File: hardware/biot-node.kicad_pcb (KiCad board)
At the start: 2 copper layers, 36.8 x 29 mm, 11 parts, among them J1 MPU9250 connection, J2 3.3V DC, P1 ATSAMR21B, P2 ATSAMR21B-TEST-POINTs, P3 ATMEL-CORTEX, P4 FTDI/Serial, SW1 Reset

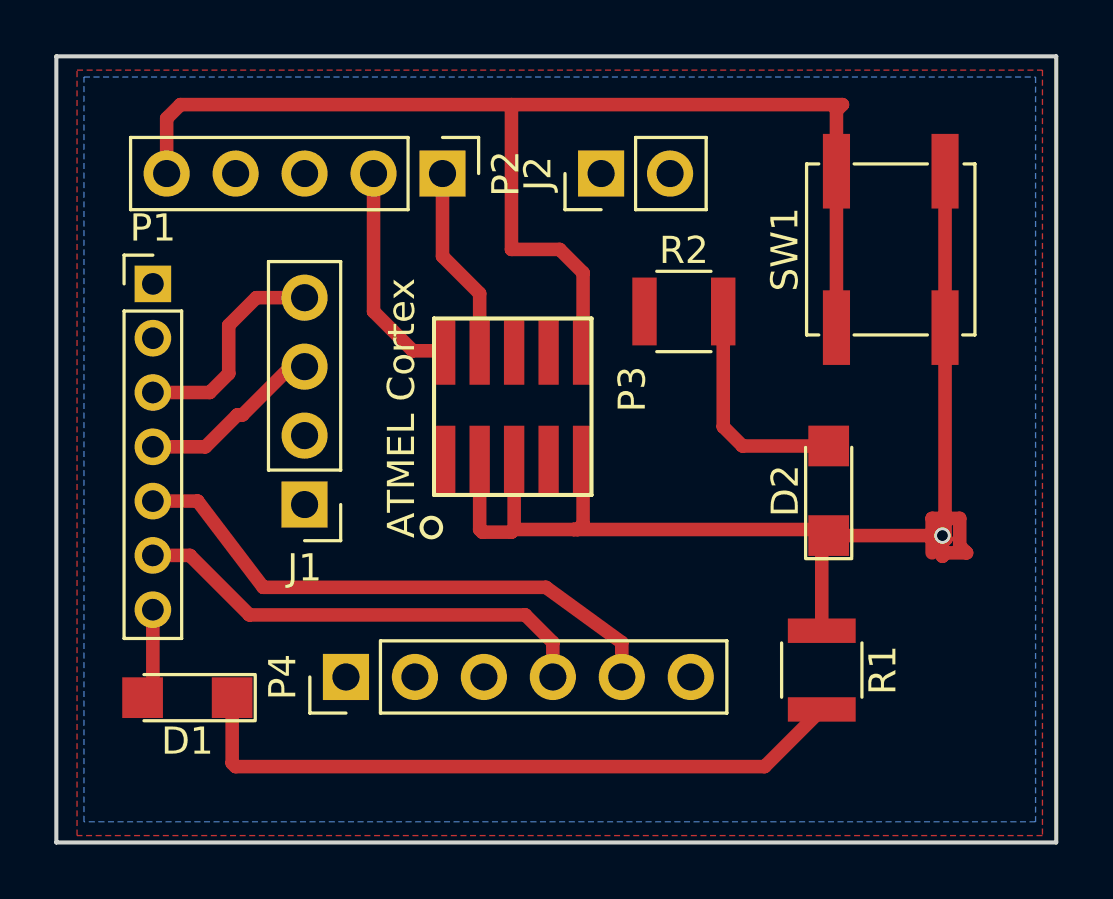
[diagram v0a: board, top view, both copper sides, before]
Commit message: Modifying PCB to suit my fabrication tools.
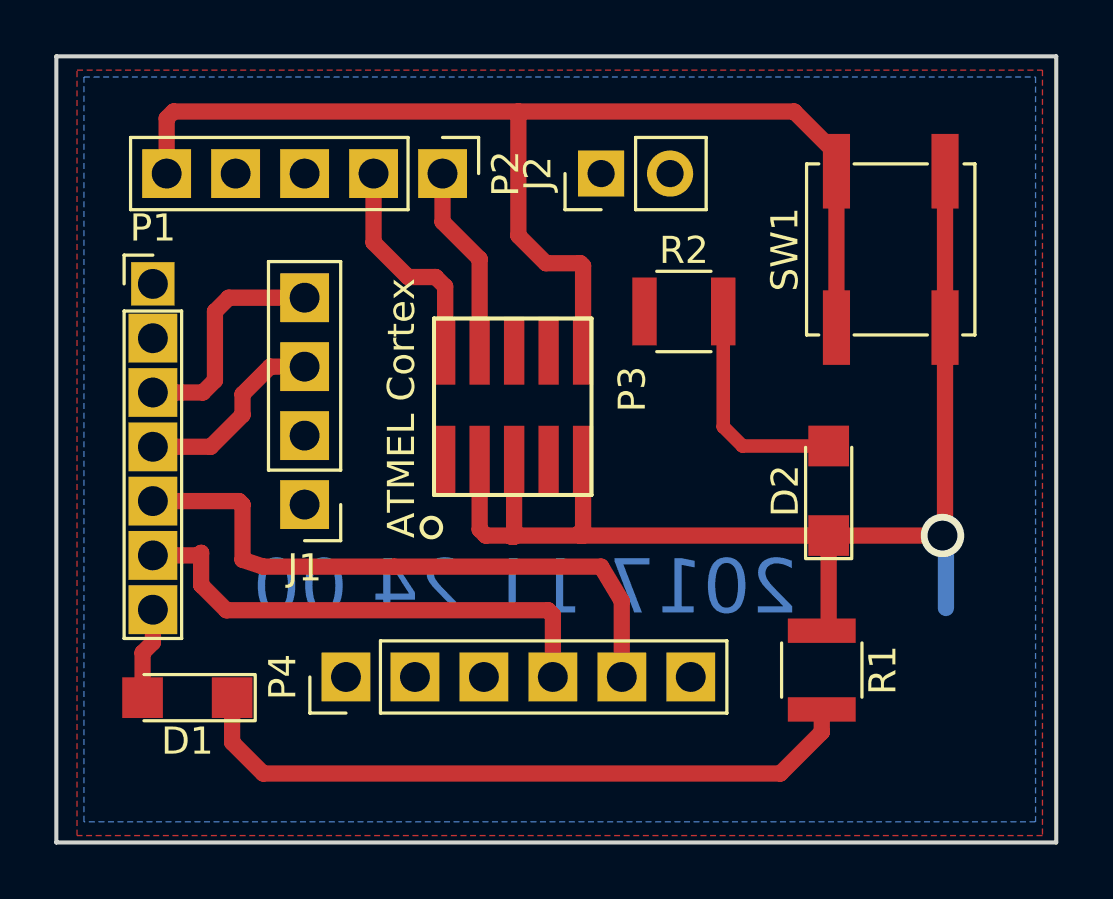
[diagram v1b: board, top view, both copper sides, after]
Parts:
- J1: footprint Pin_Headers:Pin_Header_Straight_1x04_Pitch2.54mm -> Pin_Header_Straight_1x04_Pitch2.54mm
- P1: footprint Pin_Headers:Pin_Header_Straight_1x07_Pitch2.00mm -> biotx-bits:Pin_Header_Straight_1x07_Pitch2.00mm
- P4: footprint Pin_Headers:Pin_Header_Straight_1x06_Pitch2.54mm -> Pin_Header_Straight_1x06_Pitch2.54mm
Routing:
- net RX: track 20.8 -> 23.4 mm
- net NRST: track 46.5 -> 44.5 mm
- net GND: track 48.1 -> 46.3 mm
- net TX: track 17.3 -> 18.7 mm
- net SCLK: track 6.81 -> 7.77 mm
- net Net-(D1-Pad2): track 3.40 -> 3.93 mm
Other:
- net class cnc added: clearance 0.5, trace_width 0.6, via_dia 1.6, via_drill 1.1
- board text added: "2017 11 24 00"
